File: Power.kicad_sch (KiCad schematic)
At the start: 0 parts

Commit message: power
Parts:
- added C_PWR3, C_PWR4: 1 uF, symbol Device:C_Small_US
- added U2: TPS7A2033PDBVR, TPS7A2033PDBVR:SOT95P280X145-5N, symbol TPS7A2033PDBVR_mod:TPS7A2033PDBVR
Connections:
- new net 3V3_DIG: C_PWR4.1, U2.5 (OUT)
- new net GND: C_PWR3.2, C_PWR4.2, U2.2 (GND)
- new net VBAT: C_PWR3.1, U2.1 (IN), U2.3 (EN)

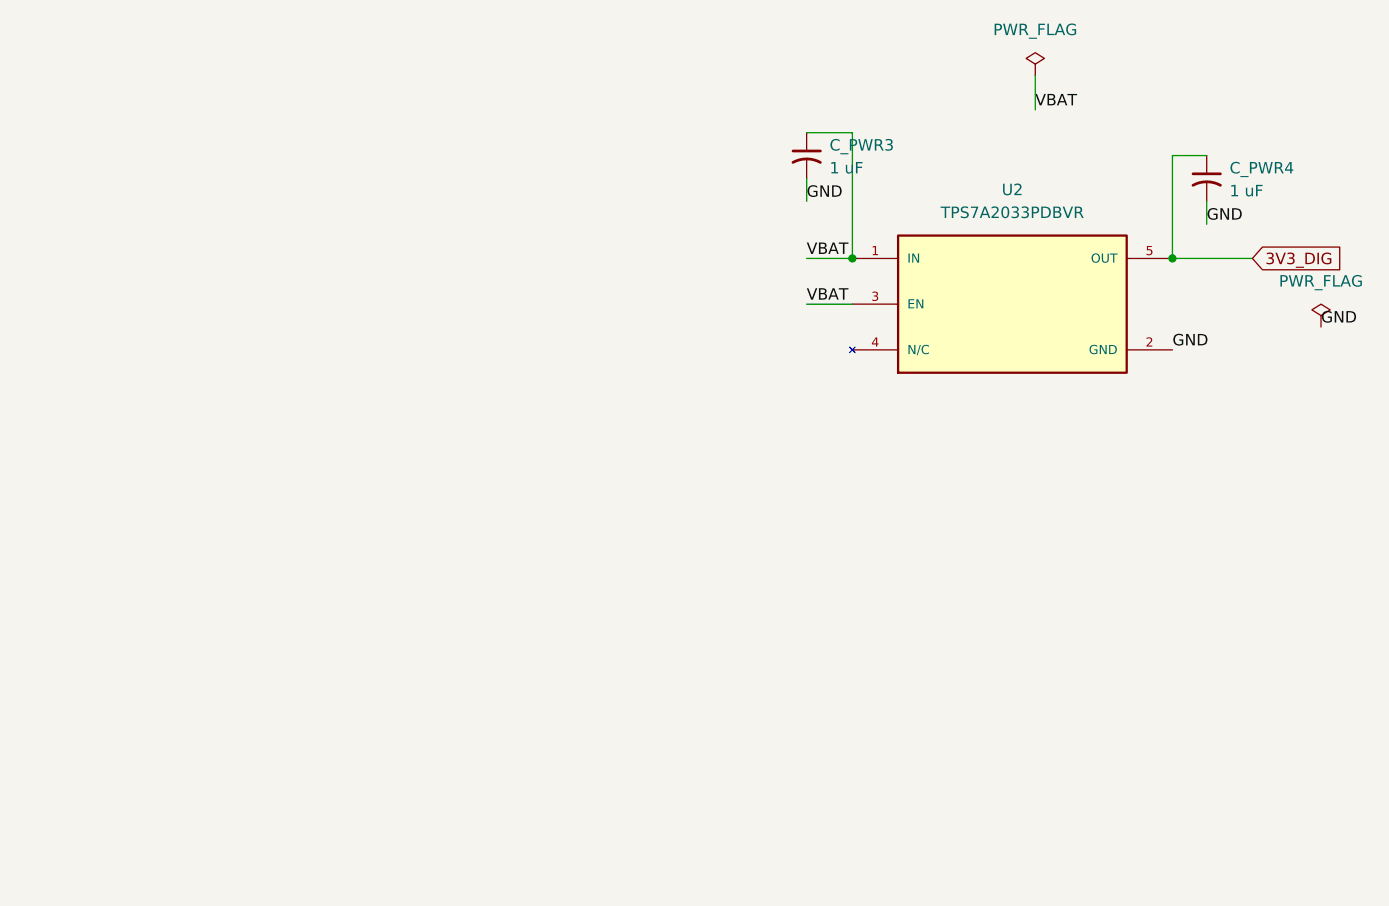
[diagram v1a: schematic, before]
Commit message: acc_power connector
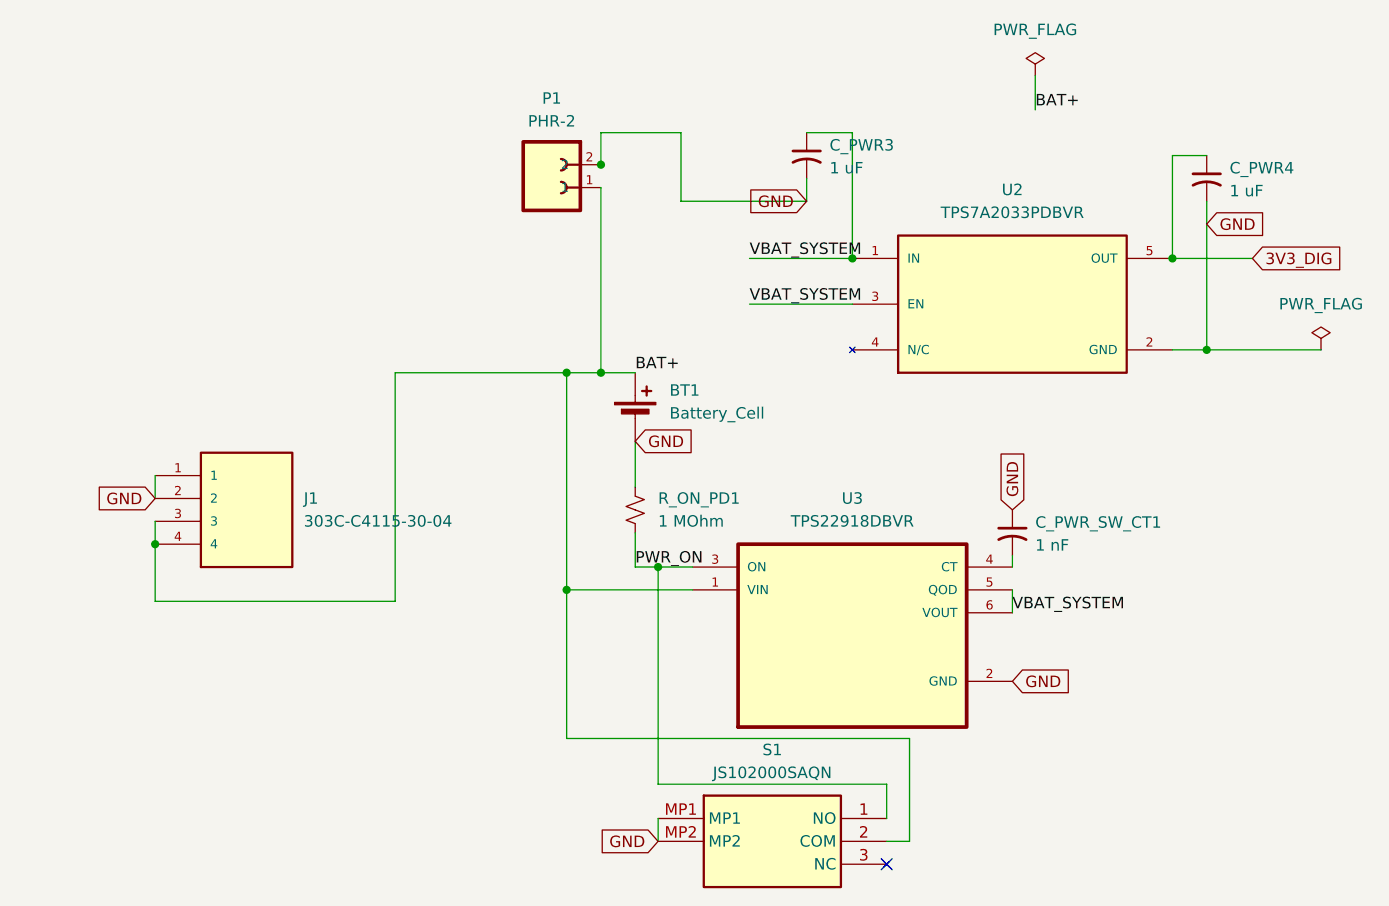
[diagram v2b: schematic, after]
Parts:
- added BT1: Battery_Cell, symbol Battery_Cell:Battery_Cell
- added C_PWR_SW_CT1: 1 nF, symbol C_Small_US:C_Small_US
- added J1: 303C-C4115-30-04, LightFusion:ATTEND_303C-C4115-30-04, symbol 303C-C4115-30-04:303C-C4115-30-04
- added P1: PHR-2, PHR-2:JST_PHR-2, symbol PHR-2:PHR-2
- added R_ON_PD1: 1 MOhm, LightFusion:R_0402_1005Metric, symbol R_Small_US:R_Small_US
- added S1: JS102000SAQN, LightFusion:JS102000SAQN, symbol JS102000SAQN:JS102000SAQN
- added U3: TPS22918DBVR, LightFusion:TPS22918DBVR-6N, symbol TPS22918DBVR:TPS22918DBVR
- C_PWR3, C_PWR4: footprint (none) -> LightFusion:C_0402_1005Metric; symbol Device:C_Small_US -> C_Small_US:C_Small_US
- U2: footprint TPS7A2033PDBVR:SOT95P280X145-5N -> LightFusion:TPS7A2033PDBVR
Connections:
- net GND: now also BT1.2 (-), C_PWR_SW_CT1.1, J1.1, J1.2, P1.2, R_ON_PD1.1, S1.MP1, S1.MP2, U3.2 (GND)
- net VBAT renamed VBAT_SYSTEM
- net VBAT_SYSTEM: now also U3.5 (QOD), U3.6 (VOUT)
- new net: C_PWR_SW_CT1.2, U3.4 (CT)
- new net BAT+: BT1.1 (+), J1.3, J1.4, P1.1, S1.2 (COM), U3.1 (VIN)
- new net PWR_ON: R_ON_PD1.2, S1.1 (NO), U3.3 (ON)
- no-connect marks 0 -> 1

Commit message: error check passed
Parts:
- C_PWR_SW_CT1: footprint (none) -> LightFusion:C_0402_1005Metric
- J1: footprint LightFusion:ATTEND_303C-C4115-30-04 -> LightFusion:303D-L186F020; symbol 303C-C4115-30-04:303C-C4115-30-04 -> 303C-C4115-30-02:303C-C4115-30-02
- P1: footprint PHR-2:JST_PHR-2 -> LightFusion:SolderWire-0.5sqmm_1x02_P4.8mm_D0.9mm_OD2.3mm; symbol PHR-2:PHR-2 -> PHR-2B:S2B-PH-K-S; Height (none) -> 4.8; Manufacturer_Name (none) -> JST (JAPAN SOLDERLESS TERMINALS); Manufacturer_Part_Number (none) -> S2B-PH-K-S
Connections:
- net BAT+: now also J1.2, P1.2; no longer J1.3, J1.4, P1.1
- net GND: now also P1.1; no longer J1.2, P1.2

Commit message: placement finished on PCB
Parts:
- C_PWR3, C_PWR4, C_PWR_SW_CT1: footprint LightFusion:C_0402_1005Metric -> LightFusion:C_0603_1608Metric
- R_ON_PD1: footprint LightFusion:R_0402_1005Metric -> LightFusion:R_0603_1608Metric
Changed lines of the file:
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@@
 			)
 		)
-		(property "Footprint" "LightFusion:C_0402_1005Metric"
+		(property "Footprint" "LightFusion:C_0603_1608Metric"
 			(at 171.45 74.93 0)
 			(hide yes)
@@
 		(property "Value" "1 uF"
 			(at 129.54 73.7869 0)
+			(hide yes)
 			(show_name no)
 			(do_not_autoplace no)
@@
 			)
 		)
-		(property "Footprint" "LightFusion:C_0402_1005Metric"
+		(property "Footprint" "LightFusion:C_0603_1608Metric"
 			(at 127 72.39 0)
 			(hide yes)
@@
 		(property "Value" "1 MOhm"
 			(at 110.49 113.0299 0)
+			(hide yes)
 			(show_name no)
 			(do_not_autoplace no)
@@
 			)
 		)
-		(property "Footprint" "LightFusion:R_0402_1005Metric"
+		(property "Footprint" "LightFusion:R_0603_1608Metric"
 			(at 107.95 111.76 0)
 			(hide yes)
@@
 		(property "Value" "1 nF"
 			(at 152.4 115.6969 0)
+			(hide yes)
 			(show_name no)
 			(do_not_autoplace no)
@@
 			)
 		)
-		(property "Footprint" "LightFusion:C_0402_1005Metric"
+		(property "Footprint" "LightFusion:C_0603_1608Metric"
 			(at 149.86 114.3 0)
 			(hide yes)

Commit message: final verifications
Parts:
- S1: Height 1.1 -> (none)
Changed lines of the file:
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@@
 			)
 		)
-		(property "Description" "capacitor, small US symbol"
+		(property "Description" ""
 			(at 171.45 74.93 0)
 			(hide yes)
@@
 			)
 		)
-		(property "Height" "1.1"
-			(at 132.08 540.97 0)
-			(hide yes)
-			(show_name no)
-			(do_not_autoplace no)
-			(effects
-				(font
-					(size 1.27 1.27)
-				)
-				(justify left top)
-			)
-		)
 		(property "Mouser Part Number" "611-JS102000SAQN"
 			(at 132.08 640.97 0)
@@
 		(fields_autoplaced yes)
 		(property "Reference" "C_PWR3"
-			(at 129.54 71.2469 0)
+			(at 129.54 72.5169 0)
 			(show_name no)
 			(do_not_autoplace no)
@@
 			)
 		)
-		(property "Description" "capacitor, small US symbol"
+		(property "Description" ""
 			(at 127 72.39 0)
 			(hide yes)
@@
 		(fields_autoplaced yes)
 		(property "Reference" "C_PWR_SW_CT1"
-			(at 152.4 113.1569 0)
-			(show_name no)
-			(do_not_autoplace no)
+			(at 152.4 114.4269 0)
+			(show_name no)
+			(do_not_autoplace no)

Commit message: All schematic and pcb checks passed
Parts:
- S1: Manufacturer_Name LITTELFUSE -> (none); Manufacturer_Part_Number JS102000SAQN -> (none); Mouser Part Number 611-JS102000SAQN -> (none); Mouser Price/Stock https://www.mouser.co.uk/ProductDetail/CK/JS102000SAQN?qs=L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 -> (none)
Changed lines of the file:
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@@
-			)
-		)
-		(property "Mouser Part Number" "611-JS102000SAQN"
-			(at 132.08 640.97 0)
-			(hide yes)
-			(show_name no)
-			(do_not_autoplace no)
-			(effects
-				(font
-					(size 1.27 1.27)
-				)
-				(justify left top)
-			)
-		)
-		(property "Mouser Price/Stock" "https://www.mouser.co.uk/ProductDetail/CK/JS102000SAQN?qs=LgMIjt8LuD%252BZDBB6AFalEw%3D%3D"
-			(at 132.08 740.97 0)
-			(hide yes)
-			(show_name no)
-			(do_not_autoplace no)
-			(effects
-				(font
-					(size 1.27 1.27)
-				)
-				(justify left top)
-			)
-		)
-		(property "Manufacturer_Name" "LITTELFUSE"
-			(at 132.08 840.97 0)
-			(hide yes)
-			(show_name no)
-			(do_not_autoplace no)
-			(effects
-				(font
-					(size 1.27 1.27)
-				)
-				(justify left top)
-			)
-		)
-		(property "Manufacturer_Part_Number" "JS102000SAQN"
-			(at 132.08 940.97 0)
-			(hide yes)
-			(show_name no)
-			(do_not_autoplace no)
-			(effects
-				(font
-					(size 1.27 1.27)
-				)
-				(justify left top)
 			)
 		)
